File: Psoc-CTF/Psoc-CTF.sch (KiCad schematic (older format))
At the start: 53 parts, among them P1 Power, P2 Analog, P3 Digital, P4 Digital, P5 CONN_01X01, P6 CONN_01X01, P7 CONN_01X01, P8 CONN_01X01

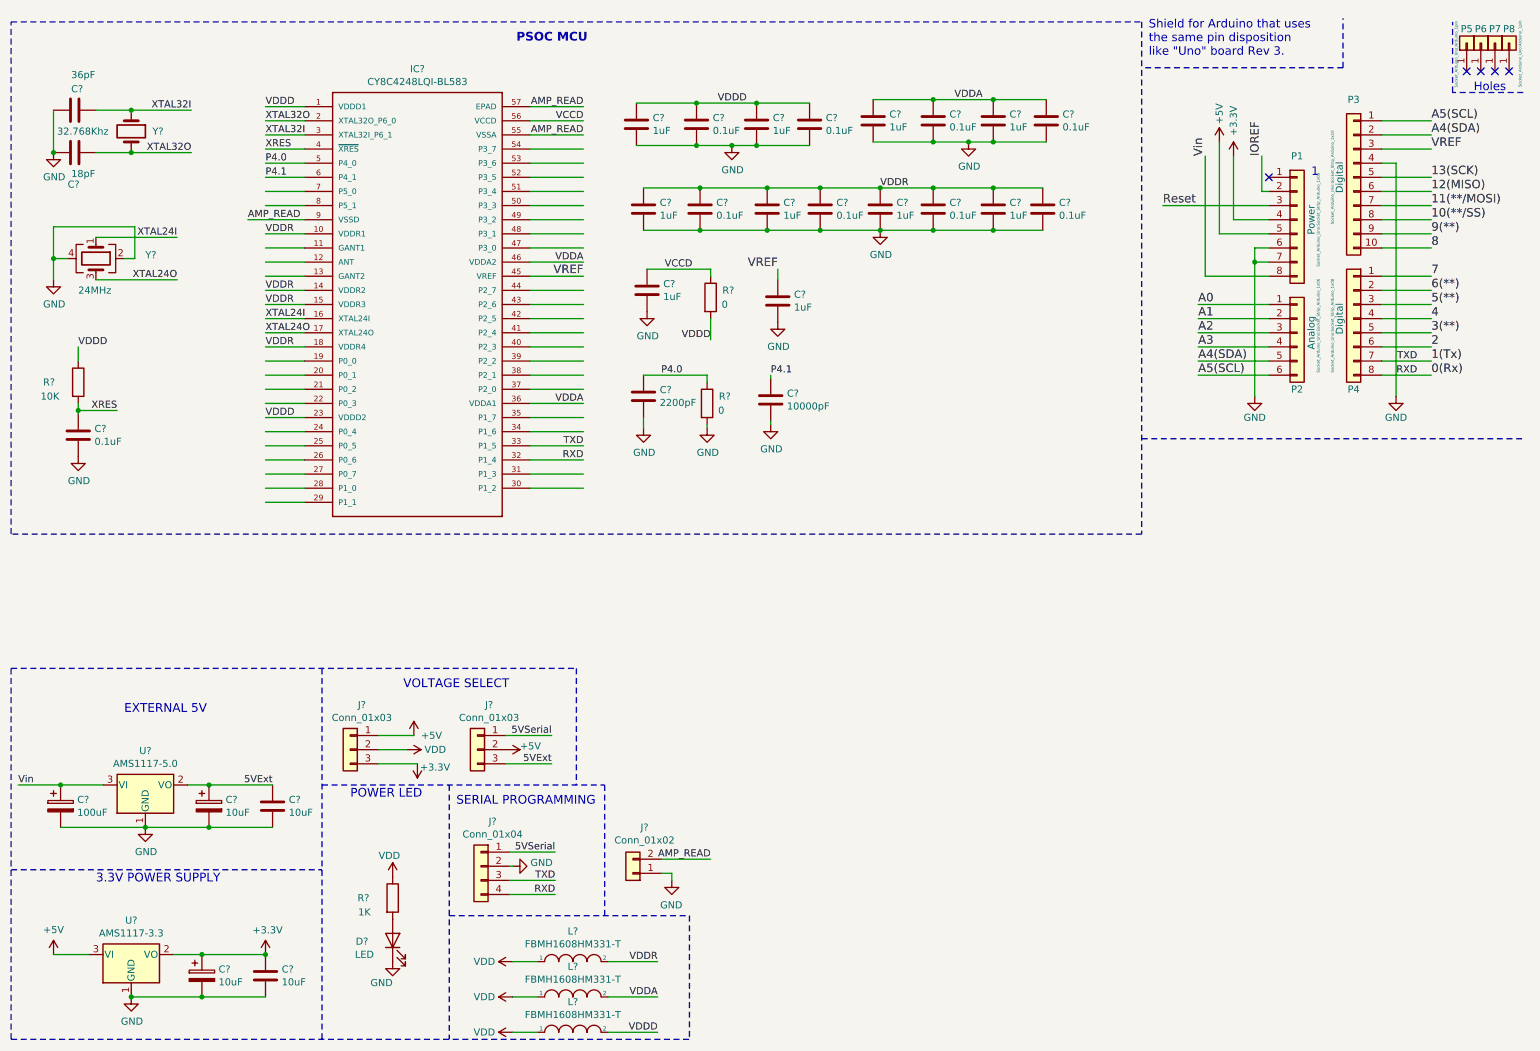
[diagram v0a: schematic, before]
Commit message: Implementación de hojas jerarquicas
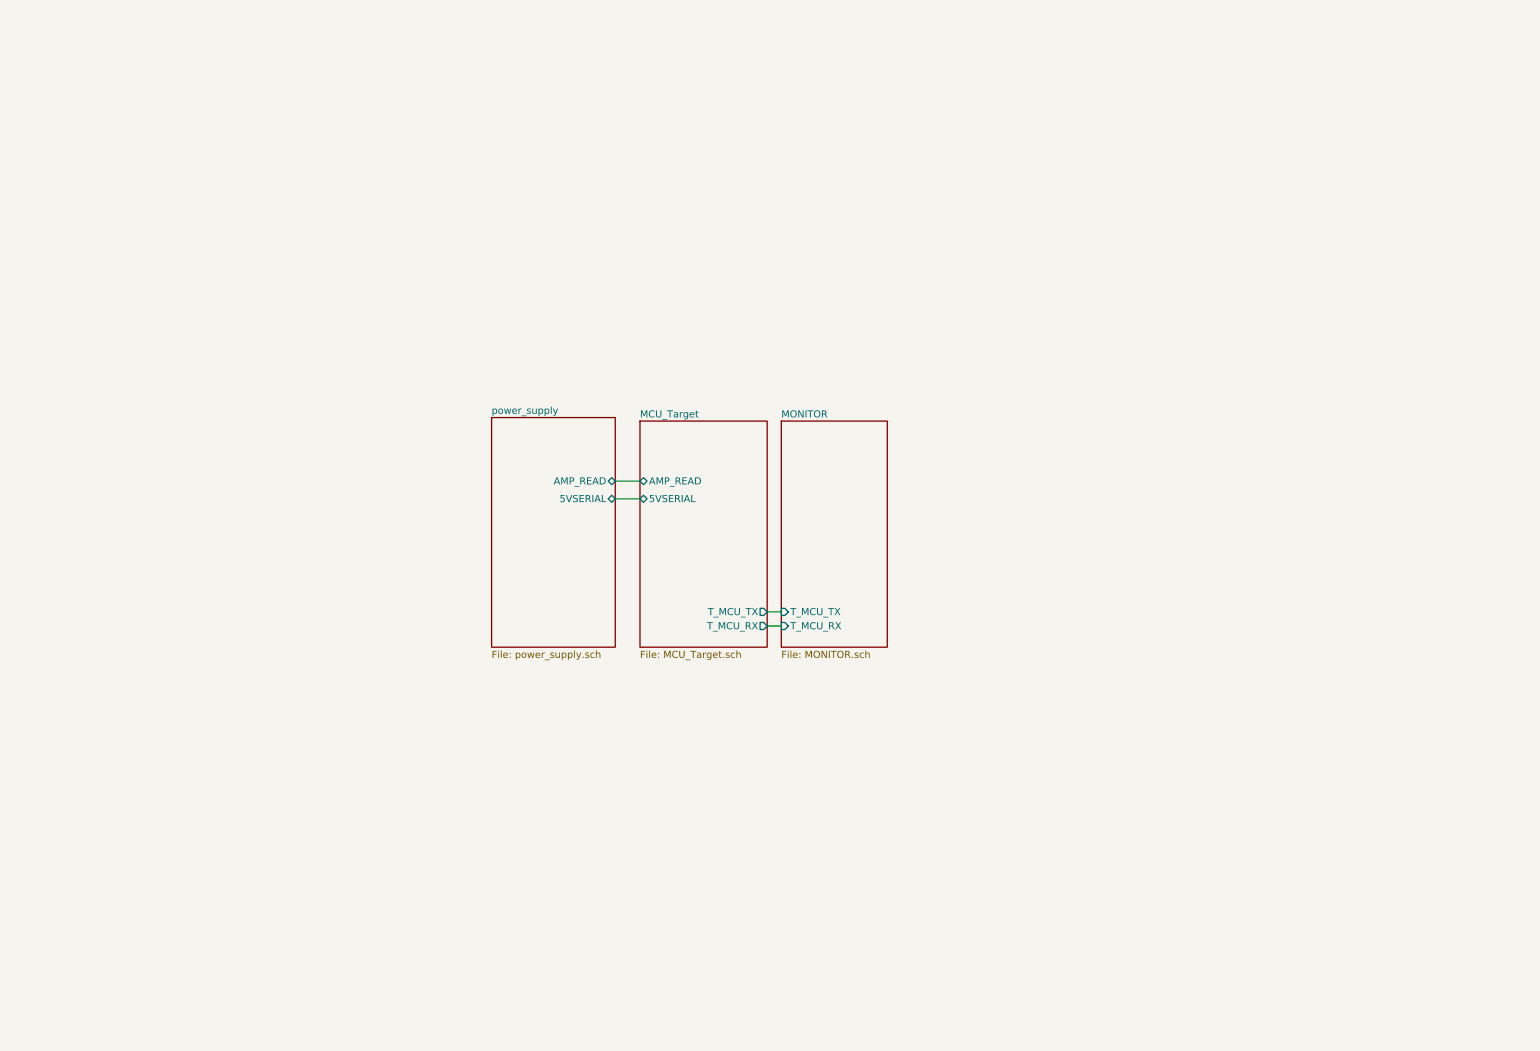
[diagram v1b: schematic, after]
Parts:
- removed C?: 36pF, Capacitor_SMD:C_0603_1608Metric_Pad1.08x0.95mm_HandSolder, symbol Device:C
- removed C?: 18pF, Capacitor_SMD:C_0603_1608Metric_Pad1.08x0.95mm_HandSolder, symbol Device:C
- removed C? (x2): 10uF, Capacitor_SMD:C_0603_1608Metric_Pad1.08x0.95mm_HandSolder, symbol Device:C
- removed C?: 100uF, Capacitor_SMD:C_0805_2012Metric_Pad1.18x1.45mm_HandSolder, symbol Device:CP
- removed C? (x2): 10uF, Capacitor_SMD:C_0805_2012Metric_Pad1.18x1.45mm_HandSolder, symbol Device:CP
- removed C? (x9): 0.1uF, Capacitor_SMD:C_0603_1608Metric_Pad1.08x0.95mm_HandSolder, symbol Device:C
- removed C? (x10): 1uF, Capacitor_SMD:C_0603_1608Metric_Pad1.08x0.95mm_HandSolder, symbol Device:C
- removed C?: 2200pF, Capacitor_SMD:C_0603_1608Metric_Pad1.08x0.95mm_HandSolder, symbol Device:C
- removed C?: 10000pF, Capacitor_SMD:C_0603_1608Metric_Pad1.08x0.95mm_HandSolder, symbol Device:C
- removed D?: LED, symbol Device:LED
- removed IC?: CY8C4248LQI-BL583, Psoc-CTF:QFN40P700X700X60-57N, symbol CY8C4248LQI-BL583:CY8C4248LQI-BL583
- removed J? (x2): Conn_01x03, symbol Connector_Generic:Conn_01x03
- removed J?: Conn_01x04, symbol Connector_Generic:Conn_01x04
- removed J?: Conn_01x02, symbol Connector_Generic:Conn_01x02
- removed L? (x3): FBMH1608HM331-T, Resistor_SMD:R_0603_1608Metric_Pad0.98x0.95mm_HandSolder, symbol pspice:INDUCTOR
- removed P1: Power, Socket_Arduino_Uno:Socket_Strip_Arduino_1x08, symbol Connector_Generic:Conn_01x08
- removed P2: Analog, Socket_Arduino_Uno:Socket_Strip_Arduino_1x06, symbol Connector_Generic:Conn_01x06
- removed P3: Digital, Socket_Arduino_Uno:Socket_Strip_Arduino_1x10, symbol Connector_Generic:Conn_01x10
- removed P4: Digital, Socket_Arduino_Uno:Socket_Strip_Arduino_1x08, symbol Connector_Generic:Conn_01x08
- removed P5, P6, P7, P8: CONN_01X01, Socket_Arduino_Uno:Arduino_1pin, symbol Connector_Generic:Conn_01x01
- removed R?: 10K, Resistor_SMD:R_0603_1608Metric_Pad0.98x0.95mm_HandSolder, symbol Device:R
- removed R?: 1K, Resistor_SMD:R_0603_1608Metric_Pad0.98x0.95mm_HandSolder, symbol Device:R
- removed R? (x2): 0, Resistor_SMD:R_0603_1608Metric_Pad0.98x0.95mm_HandSolder, symbol Device:R
- removed U?: AMS1117-5.0, Package_TO_SOT_SMD:SOT-223-3_TabPin2, symbol Regulator_Linear:AMS1117-5.0
- removed U?: AMS1117-3.3, Package_TO_SOT_SMD:SOT-223-3_TabPin2, symbol Regulator_Linear:AMS1117-3.3
- removed Y?: 32.768Khz, symbol Device:Crystal
- removed Y?: 24MHz, symbol Device:Crystal_GND24
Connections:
- net labels removed: +3.3V, +5V, 0(Rx), 1(Tx), 10(**/SS), 11(**/MOSI), 12(MISO), 13(SCK), 2, 3(**), 4, 5(**), 5VExt, 5VSerial, 6(**), 7, 8, 9(**), A0, A1, A2, A3, A4(SDA), A5(SCL), AMP_READ, GND, IOREF, P4.0, P4.1, RXD, Reset, TXD, VCCD, VDD, VDDA, VDDD, VDDR, VREF, Vin, XRES, XTAL24I, XTAL24O, XTAL32I, XTAL32O
- wire segments 180 -> 4
- no-connect marks 5 -> 0
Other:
- note removed: "1"
- note removed: "3.3V POWER SUPPLY"
- note removed: "EXTERNAL 5V"
- note removed: "Holes"
- note removed: "POWER LED"
- note removed: "PSOC MCU"
- note removed: "SERIAL PROGRAMMING"
- note removed: "Shield for Arduino that uses\nthe same pin disposition\nlike "Uno" board Rev 3."
- note removed: "VOLTAGE SELECT"

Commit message: Archivo Cache para cadlab
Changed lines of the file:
@@
 F2 "AMP_READ" B R 4775 3750 50
 F3 "5VSERIAL" B R 4775 3875 50
+F4 "Vin" I R 4775 3975 50
 $EndSheet
 $Sheet
@@
 F4 "T_MCU_RX" O R 5850 4775 50
 F5 "T_MCU_TX" O R 5850 4675 50
+F6 "Vin" I L 4950 3975 50
 $EndSheet
 Wire Wire Line
@@
 Wire Wire Line
 	4775 3875 4950 3875
+Wire Wire Line
+	4775 3975 4950 3975
 $EndSCHEMATC

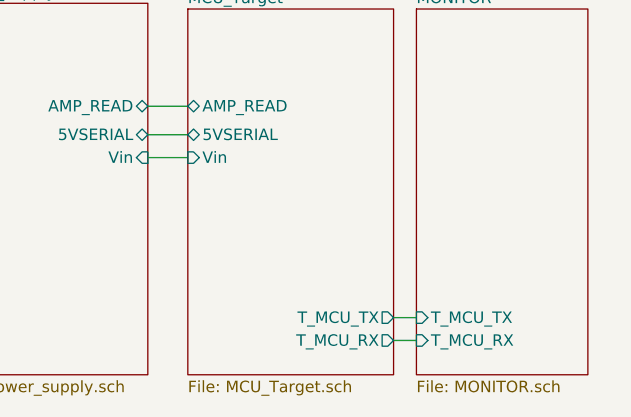
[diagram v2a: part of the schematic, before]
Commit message: Se retira las memorias flash y Ram por spi y se coloca una F-RAM por i2c
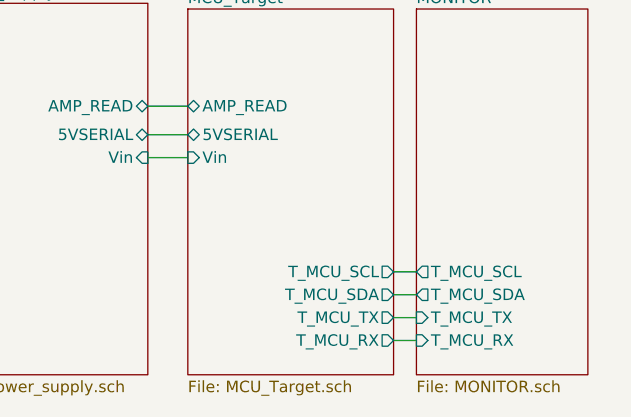
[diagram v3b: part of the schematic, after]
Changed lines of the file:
@@
 F2 "T_MCU_RX" I L 5950 4775 50
 F3 "T_MCU_TX" I L 5950 4675 50
+F4 "T_MCU_SDA" O L 5950 4575 50
+F5 "T_MCU_SCL" O L 5950 4475 50
 $EndSheet
 $Sheet
@@
 F5 "T_MCU_TX" O R 5850 4675 50
 F6 "Vin" I L 4950 3975 50
+F7 "T_MCU_SDA" O R 5850 4575 50
+F8 "T_MCU_SCL" O R 5850 4475 50
 $EndSheet
 Wire Wire Line
@@
 Wire Wire Line
 	4775 3975 4950 3975
+Wire Wire Line
+	5850 4475 5950 4475
+Wire Wire Line
+	5850 4575 5950 4575
 $EndSCHEMATC

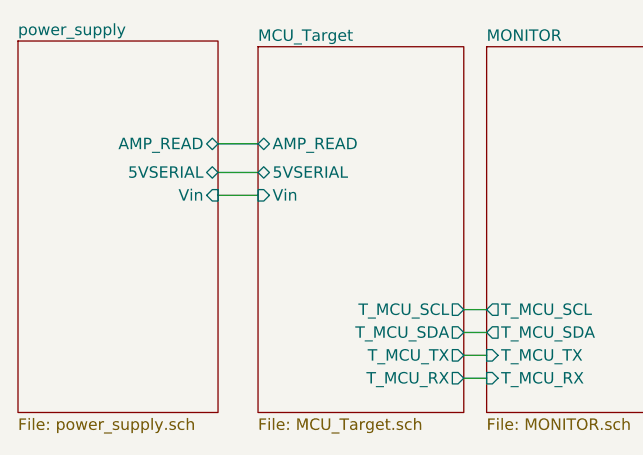
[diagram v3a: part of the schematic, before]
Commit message: Antena agregada, pines de programación SWD
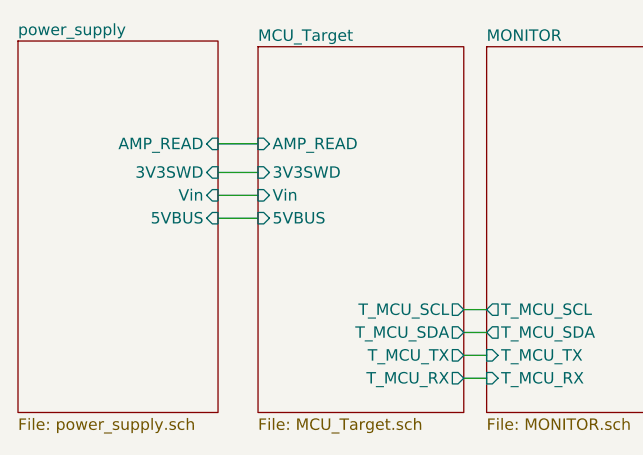
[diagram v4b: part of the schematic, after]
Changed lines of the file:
@@
 F0 "power_supply" 50
 F1 "power_supply.sch" 50
-F2 "AMP_READ" B R 4775 3750 50
-F3 "5VSERIAL" B R 4775 3875 50
-F4 "Vin" I R 4775 3975 50
+F2 "AMP_READ" I R 4775 3750 50
+F3 "Vin" I R 4775 3975 50
+F4 "3V3SWD" I R 4775 3875 50
+F5 "5VBUS" I R 4775 4075 50
 $EndSheet
 $Sheet
@@
 F0 "MCU_Target" 50
 F1 "MCU_Target.sch" 50
-F2 "AMP_READ" B L 4950 3750 50
-F3 "5VSERIAL" B L 4950 3875 50
-F4 "T_MCU_RX" O R 5850 4775 50
-F5 "T_MCU_TX" O R 5850 4675 50
-F6 "Vin" I L 4950 3975 50
-F7 "T_MCU_SDA" O R 5850 4575 50
-F8 "T_MCU_SCL" O R 5850 4475 50
+F2 "AMP_READ" I L 4950 3750 50
+F3 "T_MCU_RX" O R 5850 4775 50
+F4 "T_MCU_TX" O R 5850 4675 50
+F5 "Vin" I L 4950 3975 50
+F6 "T_MCU_SDA" O R 5850 4575 50
+F7 "T_MCU_SCL" O R 5850 4475 50
+F8 "3V3SWD" I L 4950 3875 50
+F9 "5VBUS" I L 4950 4075 50
 $EndSheet
 Wire Wire Line
@@
 Wire Wire Line
 	5850 4575 5950 4575
+Wire Wire Line
+	4775 4075 4950 4075
 $EndSCHEMATC

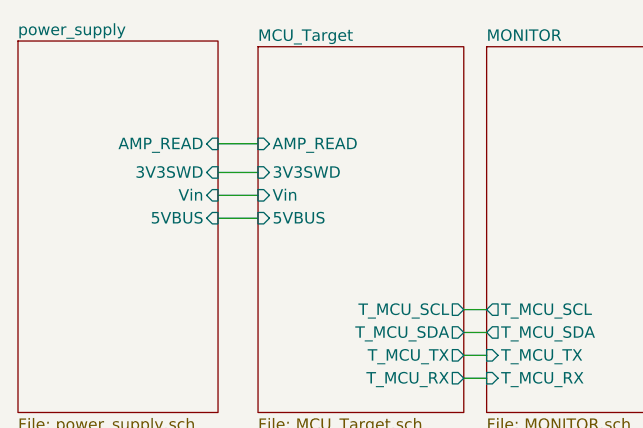
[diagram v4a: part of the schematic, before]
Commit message: Anexo de nuevos pulsadores y arreglo de resistencias
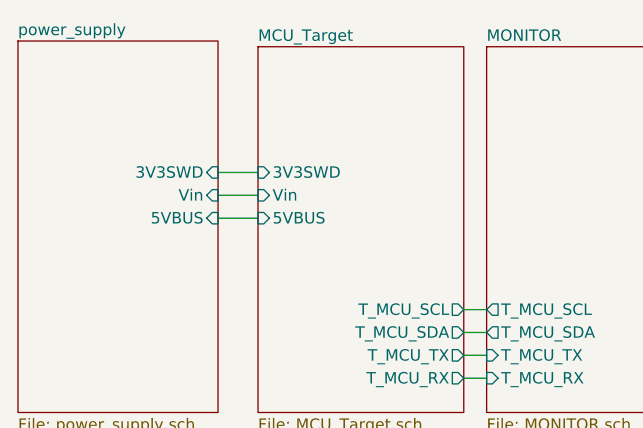
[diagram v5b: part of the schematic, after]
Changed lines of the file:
@@
 F0 "power_supply" 50
 F1 "power_supply.sch" 50
-F2 "AMP_READ" I R 4775 3750 50
-F3 "Vin" I R 4775 3975 50
-F4 "3V3SWD" I R 4775 3875 50
-F5 "5VBUS" I R 4775 4075 50
+F2 "Vin" I R 4775 3975 50
+F3 "3V3SWD" I R 4775 3875 50
+F4 "5VBUS" I R 4775 4075 50
 $EndSheet
 $Sheet
@@
 F0 "MCU_Target" 50
 F1 "MCU_Target.sch" 50
-F2 "AMP_READ" I L 4950 3750 50
-F3 "T_MCU_RX" O R 5850 4775 50
-F4 "T_MCU_TX" O R 5850 4675 50
-F5 "Vin" I L 4950 3975 50
-F6 "T_MCU_SDA" O R 5850 4575 50
-F7 "T_MCU_SCL" O R 5850 4475 50
-F8 "3V3SWD" I L 4950 3875 50
-F9 "5VBUS" I L 4950 4075 50
+F2 "T_MCU_RX" O R 5850 4775 50
+F3 "T_MCU_TX" O R 5850 4675 50
+F4 "Vin" I L 4950 3975 50
+F5 "T_MCU_SDA" O R 5850 4575 50
+F6 "T_MCU_SCL" O R 5850 4475 50
+F7 "3V3SWD" I L 4950 3875 50
+F8 "5VBUS" I L 4950 4075 50
 $EndSheet
 Wire Wire Line
@@
 	5850 4775 5950 4775
 Wire Wire Line
-	4775 3750 4950 3750
-Wire Wire Line
 	4775 3875 4950 3875

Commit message: Ruteo Psoc-CTF
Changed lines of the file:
@@
 F0 "power_supply" 50
 F1 "power_supply.sch" 50
-F2 "Vin" I R 4775 3975 50
-F3 "3V3SWD" I R 4775 3875 50
-F4 "5VBUS" I R 4775 4075 50
+F2 "3V3SWD" I R 4775 3875 50
+F3 "VBUS" I R 4775 4000 50
 $EndSheet
 $Sheet
@@
 F4 "T_MCU_SDA" O L 5950 4575 50
 F5 "T_MCU_SCL" O L 5950 4475 50
+F6 "VBUS" I R 6700 4000 50
 $EndSheet
 $Sheet
@@
 F2 "T_MCU_RX" O R 5850 4775 50
 F3 "T_MCU_TX" O R 5850 4675 50
-F4 "Vin" I L 4950 3975 50
-F5 "T_MCU_SDA" O R 5850 4575 50
-F6 "T_MCU_SCL" O R 5850 4475 50
-F7 "3V3SWD" I L 4950 3875 50
-F8 "5VBUS" I L 4950 4075 50
+F4 "T_MCU_SDA" O R 5850 4575 50
+F5 "T_MCU_SCL" O R 5850 4475 50
+F6 "3V3SWD" I L 4950 3875 50
+F7 "VBUS" I L 4950 4000 50
 $EndSheet
 Wire Wire Line
@@
 	4775 3875 4950 3875
 Wire Wire Line
-	4775 3975 4950 3975
-Wire Wire Line
 	5850 4475 5950 4475
 Wire Wire Line
 	5850 4575 5950 4575
 Wire Wire Line
-	4775 4075 4950 4075
+	4775 4000 4850 4000
+Wire Wire Line
+	6700 4000 6975 4000
+Wire Wire Line
+	6975 4000 6975 5075
+Wire Wire Line
+	6975 5075 4850 5075
+Wire Wire Line
+	4850 5075 4850 4000
+Connection ~ 4850 4000
+Wire Wire Line
+	4850 4000 4950 4000
 $EndSCHEMATC
